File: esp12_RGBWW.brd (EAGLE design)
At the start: 53 x 47 mm, 36 parts, among them Q1 AOD2910SMD, Q2 AOD2910SMD, Q3 AOD2910SMD, Q4 AOD2910SMD, Q5 AOD2910SMD, U1 TPS5410DR

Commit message: added fhem logo and reference
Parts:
- added U$1: (no value), fhem.logo:LOGO
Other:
- board text added: "Lightinator 3, brought to you by the fhem community http://forum.fhem.de"
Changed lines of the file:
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@@
 <layer number="100" name="Muster" color="7" fill="1" visible="no" active="no"/>
 <layer number="118" name="Rect_Pads" color="7" fill="1" visible="no" active="no"/>
+<layer number="200" name="200bmp" color="1" fill="10" visible="yes" active="yes"/>
 <layer number="217" name="217bmp" color="18" fill="1" visible="no" active="no"/>
 <layer number="218" name="218bmp" color="19" fill="1" visible="no" active="no"/>
@@
 <wire x1="22.86" y1="27.94" x2="22.225" y2="27.305" width="0.254" layer="25"/>
 <wire x1="25.4" y1="27.94" x2="26.035" y2="28.575" width="0.254" layer="25"/>
+<text x="18.415" y="29.845" size="1.016" layer="26" rot="MR0">Lightinator 3, brought to you
+by the fhem community
+http://forum.fhem.de</text>
 </plain>
 <attributes>
@@
 <attribute name="VALUE" x="22.86" y="23.495" size="1.27" layer="27"/>
 </element>
+<element name="U$1" library="fhem.logo" package="LOGO" value="" x="39.37" y="22.86" rot="MR0"/>
 </elements>
 <signals>
@@
 </board>
 </drawing>
+<compatibility>
+<note version="6.3" minversion="6.2.2" severity="warning">
+Since Version 6.2.2 text objects can contain more than one line,
+which will not be processed correctly with this version.
+</note>
+</compatibility>
 </eagle>

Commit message: final production version
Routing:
- net GND: track 58.4 -> 57.1 mm
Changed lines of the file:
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@@
 <wire x1="22.86" y1="27.94" x2="22.225" y2="27.305" width="0.254" layer="25"/>
 <wire x1="25.4" y1="27.94" x2="26.035" y2="28.575" width="0.254" layer="25"/>
-<text x="18.415" y="29.845" size="1.016" layer="26" rot="MR0">Lightinator 3, brought to you
+<text x="18.415" y="29.845" size="0.8128" layer="26" font="vector" rot="MR0">Lightinator 3, brought to you
 by the fhem community
 http://forum.fhem.de</text>
@@
 <contactref element="VCC" pad="2"/>
 <via x="16.51" y="14.605" extent="1-16" drill="0.6"/>
-<wire x1="14.92" y1="8.89" x2="13.65" y2="10.16" width="0.4064" layer="1"/>
-<wire x1="13.65" y1="10.16" x2="13.65" y2="9.84" width="0.4064" layer="1"/>
-<wire x1="13.65" y1="9.84" x2="12.7" y2="8.89" width="0.4064" layer="1"/>
 <wire x1="16.51" y1="14.605" x2="17.685" y2="13.43" width="0.6096" layer="1"/>
 <wire x1="17.685" y1="13.43" x2="18.74" y2="13.43" width="0.6096" layer="1"/>
@@
 <wire x1="45.4025" y1="31.75" x2="45.4025" y2="32.995" width="0.3048" layer="1"/>
 <wire x1="45.4025" y1="32.995" x2="45.3775" y2="32.7025" width="0.3048" layer="1"/>
-<wire x1="12.7" y1="8.89" x2="7.9375" y2="8.89" width="0.4064" layer="1"/>
-<wire x1="7.9375" y1="8.89" x2="7.3" y2="9.5275" width="0.4064" layer="1"/>
-<wire x1="7.3" y1="9.5275" x2="7.3" y2="10.16" width="0.4064" layer="1"/>
 <wire x1="26.9625" y1="32.7025" x2="25.4" y2="32.7025" width="0.3048" layer="1"/>
 <wire x1="25.4" y1="32.7025" x2="25.0825" y2="33.02" width="0.3048" layer="1"/>
@@
 <vertex x="0" y="7.62"/>
 </polygon>
-<wire x1="14.92" y1="8.89" x2="21.9075" y2="8.89" width="0.4064" layer="1"/>
-<wire x1="21.9075" y1="8.89" x2="22.70125" y2="9.68375" width="0.4064" layer="1"/>
-<wire x1="22.70125" y1="9.68375" x2="22.8575" y2="9.84" width="0.4064" layer="1"/>
-<wire x1="22.8575" y1="9.84" x2="22.8575" y2="11.1125" width="0.4064" layer="1"/>
+<wire x1="7.9375" y1="8.89" x2="13.81125" y2="8.89" width="0.4064" layer="1"/>
+<wire x1="13.81125" y1="8.89" x2="22.86" y2="8.89" width="0.4064" layer="1"/>
 <wire x1="30.1625" y1="11.4275" x2="30.1625" y2="9.8425" width="0.4064" layer="1"/>
 <wire x1="30.1625" y1="9.8425" x2="29.21" y2="8.89" width="0.4064" layer="1"/>
-<wire x1="29.21" y1="8.89" x2="23.495" y2="8.89" width="0.4064" layer="1"/>
-<wire x1="23.495" y1="8.89" x2="22.70125" y2="9.68375" width="0.4064" layer="1"/>
+<wire x1="29.21" y1="8.89" x2="22.86" y2="8.89" width="0.4064" layer="1"/>
 <contactref element="PRG" pad="2"/>
 <contactref element="JP1" pad="6"/>
@@
 <via x="10.16" y="21.59" extent="1-16" drill="0.6" shape="octagon"/>
 <via x="7.62" y="21.59" extent="1-16" drill="0.6" shape="octagon"/>
+<wire x1="13.65" y1="10.16" x2="13.81125" y2="10.16" width="0.4064" layer="1"/>
+<wire x1="13.81125" y1="10.16" x2="13.81125" y2="8.89" width="0.4064" layer="1"/>
+<wire x1="22.8575" y1="11.1125" x2="22.86" y2="11.1125" width="0.4064" layer="1"/>
+<wire x1="22.86" y1="11.1125" x2="22.86" y2="8.89" width="0.4064" layer="1"/>
 </signal>
 <signal name="RST_S" class="5">
@@
 <wire x1="1.524" y1="17.34" x2="0.83" y2="17.34" width="0.4064" layer="16"/>
 <wire x1="2.54" y1="15.43" x2="3.62" y2="15.43" width="0.3048" layer="1"/>
-<wire x1="3.62" y1="15.43" x2="4.445" y2="14.605" width="0.3048" layer="1"/>
-<wire x1="4.445" y1="14.605" x2="4.445" y2="10.4775" width="0.3048" layer="1"/>
+<wire x1="3.62" y1="15.43" x2="4.445" y2="14.605" width="0.4064" layer="1"/>
+<wire x1="4.445" y1="14.605" x2="4.445" y2="10.4775" width="0.4064" layer="1"/>
 <wire x1="1.524" y1="17.34" x2="1.71" y2="17.34" width="0.3048" layer="16"/>
-<wire x1="1.71" y1="17.34" x2="4.445" y2="14.605" width="0.3048" layer="16"/>
-<wire x1="4.445" y1="10.4775" x2="4.7625" y2="10.16" width="0.3048" layer="1"/>
+<wire x1="1.71" y1="17.34" x2="4.445" y2="14.605" width="0.4064" layer="16"/>
+<wire x1="4.445" y1="10.4775" x2="4.7625" y2="10.16" width="0.4064" layer="1"/>
 <wire x1="4.7625" y1="10.16" x2="5.4" y2="10.16" width="0.3048" layer="1"/>
 </signal>

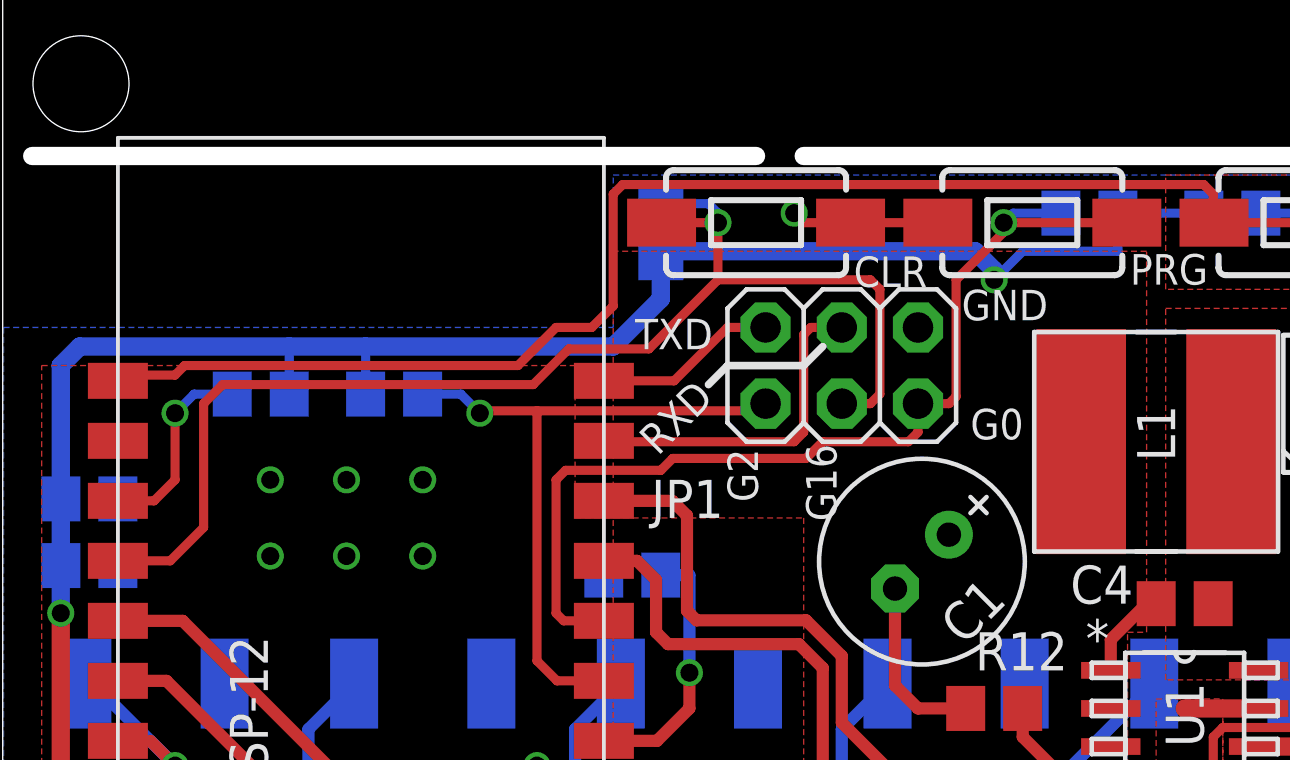
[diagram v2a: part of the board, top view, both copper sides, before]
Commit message: added VCC and G15 to pin header
in the earlier design, I had omitted a VCC pin at the pin header. That could be a useful pin for folks using the board with the TAMSOTA firmware, opening up a few pins for external sensors.
Now G0, G2, G15 and G16 are available on the header.
When using them, you should be aware that G0, G2 and G16 are internally pulled up and G15 is pulled low. depending on the loaded firmware, changing the level of those pins (especially at boot time) may trigger unintended behaviour.
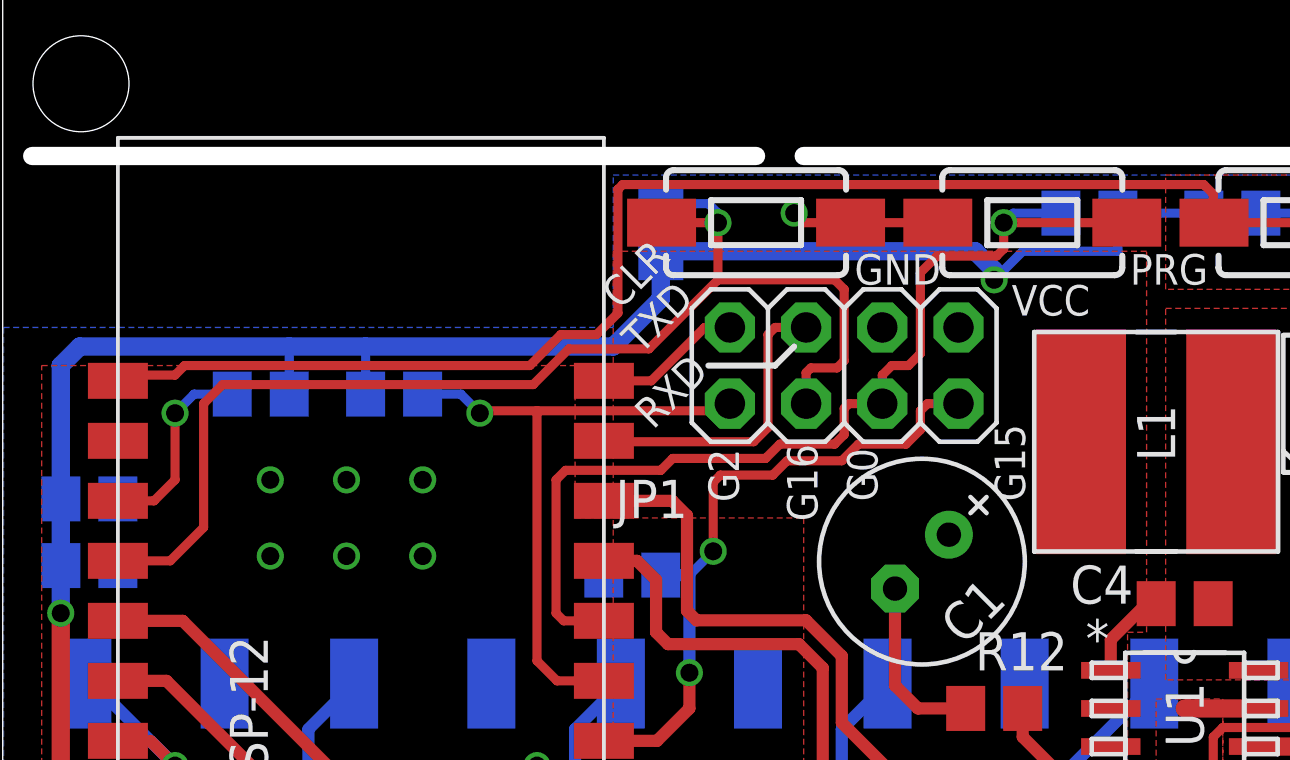
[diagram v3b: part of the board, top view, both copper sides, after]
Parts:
- JP1: device adafruit:2X03 -> adafruit:2X04
- moved JP1 1.19 mm to (26.7, 27.9)
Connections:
- net +3V3: now also JP1.8
- net G15: now also JP1.7
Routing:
- net G15: track 8.70 -> 21.8 mm, vias 1 -> 2
- net RXD: track 11.4 -> 10.1 mm
- net CLR_S: track 43.1 -> 41.9 mm
- net TXD: track 6.13 -> 4.94 mm
- net G2: track 22.7 -> 21.5 mm
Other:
- board text added: "G15"
